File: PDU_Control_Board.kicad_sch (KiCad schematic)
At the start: 267 parts

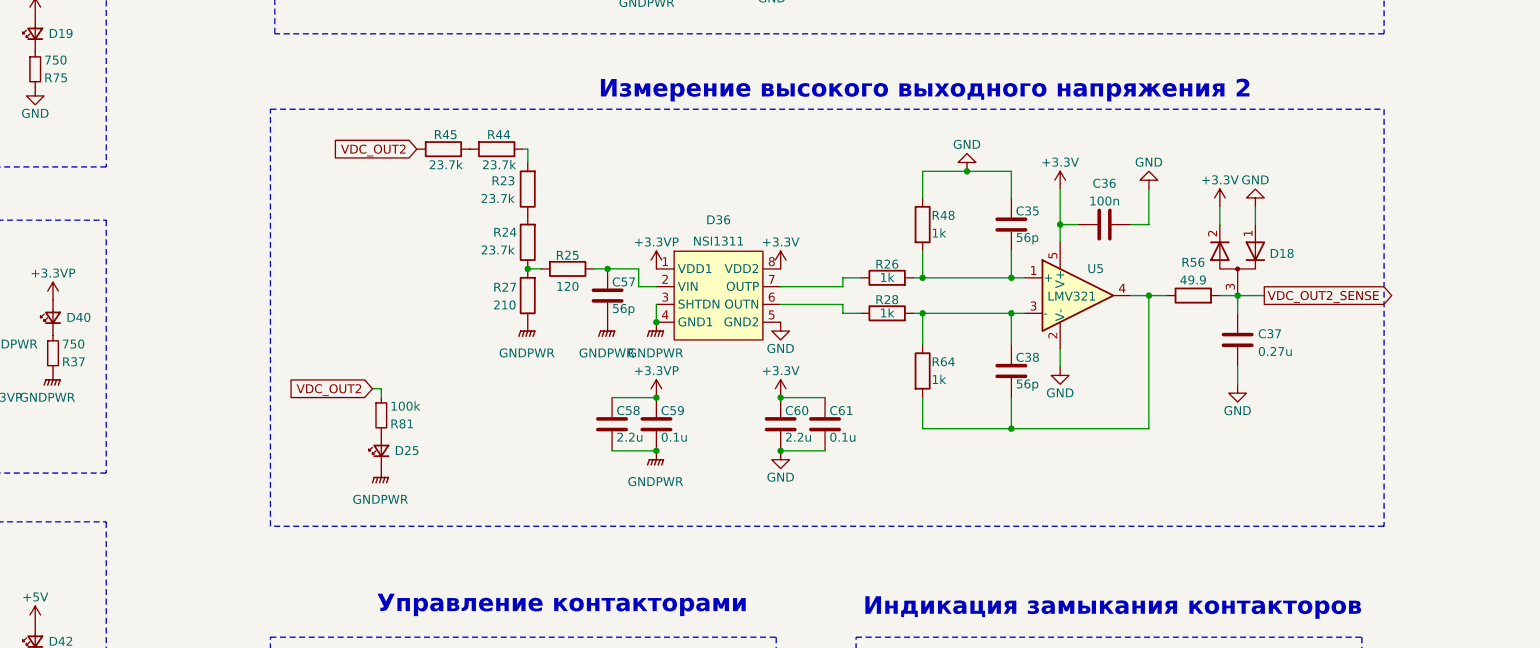
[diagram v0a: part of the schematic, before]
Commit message: VER1.1: добавил резистор смещение в измерение шины DC
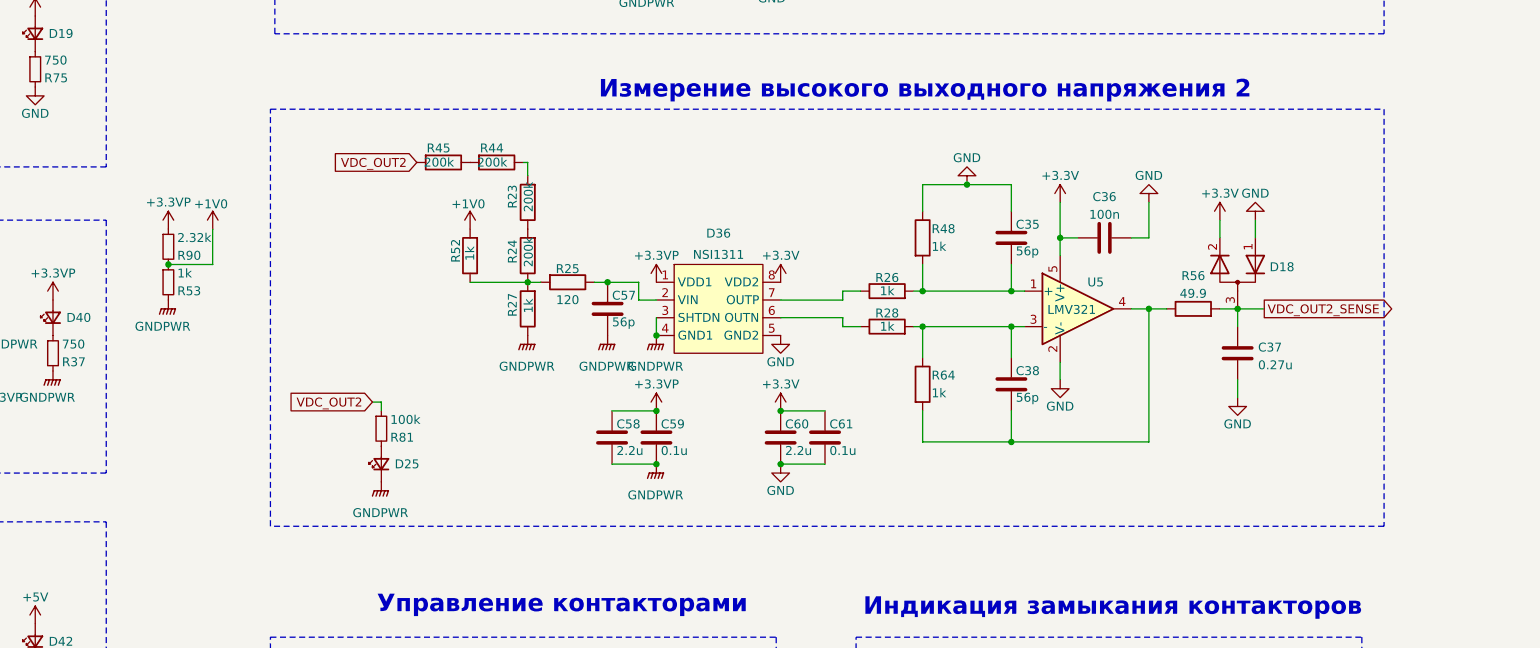
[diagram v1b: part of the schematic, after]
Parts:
- added R52: 1k, Resistor_SMD:R_1206_3216Metric, symbol Device:R
- added R53: 1k, Resistor_SMD:R_0805_2012Metric_Pad1.20x1.40mm_HandSolder, symbol Device:R_Small
- added R90: 2.32k, Resistor_SMD:R_0805_2012Metric_Pad1.20x1.40mm_HandSolder, symbol Device:R_Small
- R23, R24, R44, R45: value 23.7k -> 200k
- R27: value 210 -> 1k
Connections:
- net +3.3VP: now also R90.1
- net GNDPWR: now also R53.2
- net at R24.1, R25.2, R27.2: now also R52.1
- new net +1V0: R52.2, R53.1, R90.2
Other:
- moved on the sheet: C35, C36, C37, C38, C57, C58, C59, C60, C61, D18, D25, D36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

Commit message: VER1.2: добавил защиту по высокому
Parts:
- removed C77: 4.7u, Capacitor_SMD:C_1206_3216Metric_Pad1.33x1.80mm_HandSolder, symbol Device:C_Small
- removed C78, C79, C83: 10u, Capacitor_SMD:C_1206_3216Metric_Pad1.33x1.80mm_HandSolder, symbol Device:C_Small
- removed C80: 100n, Capacitor_SMD:C_0805_2012Metric_Pad1.18x1.45mm_HandSolder, symbol Device:C_Small
- removed C81, C82: 5.6n, Capacitor_SMD:C_0805_2012Metric_Pad1.18x1.45mm_HandSolder, symbol Device:C_Small
- removed D25, D26, D27: ~, LED_SMD:LED_0805_2012Metric, symbol Device:LED_Small
- removed D45: ~, MORNSUN:B_S-2WR3, symbol MORNSUN:A_S-2WR3
- removed D46: ~, Package_TO_SOT_SMD:SOT-23-5_HandSoldering, symbol Gate_Driver_my:RS8801HXF5
- removed D47, D48: D_Schottky_Small, symbol Device:D_Schottky_Small
- removed D49, D50: ~, Package_TO_SOT_THT:TO-220-2_Vertical, symbol Device:D_Schottky
- removed L2: 6.8u, symbol Device:L_Small
- removed L3: 560u, symbol Device:L
- removed Q12: ~, Package_TO_SOT_THT:TO-247-3_Vertical, symbol Transistor_FET:BSP129
- removed R55: 200, Resistor_SMD:R_0805_2012Metric_Pad1.20x1.40mm_HandSolder, symbol Device:R_Small
- removed R57: 13.3k, Resistor_SMD:R_0805_2012Metric_Pad1.20x1.40mm_HandSolder, symbol Device:R_Small
- removed R58: 200k, Resistor_SMD:R_0805_2012Metric_Pad1.20x1.40mm_HandSolder, symbol Device:R_Small
- removed R59: 2.37k, Resistor_SMD:R_0805_2012Metric_Pad1.20x1.40mm_HandSolder, symbol Device:R_Small
- removed R60, R63: 10k, Resistor_SMD:R_0805_2012Metric_Pad1.20x1.40mm_HandSolder, symbol Device:R_Small
- removed R61: 0.1, Resistor_SMD:R_2512_6332Metric_Pad1.40x3.35mm_HandSolder, symbol Device:R_Small
- removed R62: 0, Resistor_SMD:R_1206_3216Metric_Pad1.30x1.75mm_HandSolder, symbol Device:R_Small
- removed R81, R82, R83: 100k, Resistor_SMD:R_1206_3216Metric_Pad1.30x1.75mm_HandSolder, symbol Device:R_Small
- removed U7: ~, Package_TO_SOT_SMD:SOT-23-5_HandSoldering, symbol Comparator:LMV7219M5
- removed U8: ~, Package_TO_SOT_SMD:SOT-223-3_TabPin2, symbol Regulator_Linear:LD1117S33TR_SOT223
- added J15: ~, Connector_My:Mini-Fit_01x02_Vertical, symbol Connector_Generic:Conn_01x02
- added R55, R57: 1.6k, Resistor_SMD:R_1206_3216Metric, symbol Device:R
- C76: value 4.7u -> 100n; footprint Capacitor_SMD:C_1206_3216Metric_Pad1.33x1.80mm_HandSolder -> Capacitor_SMD:C_0805_2012Metric_Pad1.18x1.45mm_HandSolder
- R10, R11, R12, R13, R4, R5, R76, R77, R78, R79, R80: value 5.1k -> 8.2k
- R15, R16, R46, R49, R50, R51, R88, R89: value 23.7k -> 200k
- R18, R87: value 210 -> 1.6k
- R27, R52: value 1k -> 1.6k
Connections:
- net VDC_IN is gone; now on net VDC: J20.1 (Pin_1)
- net +1V0: now also C76.2, R55.2, R57.2
- net GND: no longer C76.2
- net GNDPWR: now also C76.1, J15.1 (Pin_1), J15.2 (Pin_2); no longer J20.2 (Pin_2), J21.2 (Pin_2), J22.2 (Pin_2)
- net VDC: now also J20.2 (Pin_2)
- net VDC_OUT1: now also J21.2 (Pin_2)
- net VDC_OUT2: now also J22.2 (Pin_2)
- net at R16.1, R17.2, R18.2: now also R55.1
- net at R86.2, R87.2, R88.1: now also R57.1
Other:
- note added: "Питание 1В"
- note removed: "Предзаряд электронный"
- moved on the sheet: C22, C23, C29, C30, C31, C32, C34, C47, C48, C49, C50, C51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

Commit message: VER1.2: отправил в резонит
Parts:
- D44: value BZT52C10 -> ~; Description P/N (none) -> Zener_Diode; Product Name (none) -> BZT52C10
- Q11: Product Name (none) -> 20N06
- R15, R16, R23, R24, R44, R45, R46, R49, R50, R51, R88, R89: value 200k -> 2M
- R18, R27, R52, R55, R57, R87: value 1.6k -> 16k
- R53: value 1k -> 100
- R90: value 2.32k -> 232
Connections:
- net Discete_8 is gone; now on net Discete_4: J14.8 (Pin_8), U2.46 (PE15)
- net Discete_1: now also J14.2 (Pin_2), U2.43 (PE12); no longer J14.1 (Pin_1), U2.39 (PE8)
- net Discete_2: now also J14.4 (Pin_4), U2.44 (PE13); no longer J14.2 (Pin_2), U2.40 (PE9)
- net Discete_3: now also J14.6 (Pin_6), U2.45 (PE14); no longer J14.3 (Pin_3), U2.41 (PE10)
- net Discete_4: no longer J14.4 (Pin_4), U2.42 (PE11)
- net GND: now also J14.1 (Pin_1), J14.3 (Pin_3), J14.5 (Pin_5), J14.7 (Pin_7)
- removed net Discete_5: J14.5 (Pin_5), U2.43 (PE12)
- removed net Discete_6: J14.6 (Pin_6), U2.44 (PE13)
- removed net Discete_7: J14.7 (Pin_7), U2.45 (PE14)
- no-connect marks 53 -> 57

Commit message: VER1.2: добавил КД на диск
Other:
- note added: "1. Перечень элементов см. НВЦТ.0001.0400.200 ПЭ3_v1.2"
- note added: "НВЦТ.0001.0400.200"
- note added: "ООО "Электротранспортные"
- note added: "Разъемы и механические отверстия"
- note added: "Схема электрическая принципиальная"
- note added: "технологии""
- title: (none) -> Плата управления
- moved on the sheet: C1, C10, C11, C12, C13, C14, C15, C16, C17, C18, C19, C2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

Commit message: VER1.2: исправил доки
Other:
- note added: "1. Перечень элементов см. НВЦТ.0001.0400.200 ПЭ3_v1."
- note added: "НВЦТ.0001.0400.200_v1"
- note removed: "1. Перечень элементов см. НВЦТ.0001.0400.200 ПЭ3_v1.2"
- note removed: "НВЦТ.0001.0400.200"
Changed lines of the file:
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@@
 	(title_block
 		(title "Плата управления")
-		(comment 1 "НВЦТ.0001.0400.200 Э3_v1.2")
+		(comment 1 "НВЦТ.0001.0400.200 Э3_v1 Э3")
 		(comment 2 "Филатов А.С,")
 		(comment 3 "Сизякин.А.В.")
@@
 		)
 	)
-	(text "НВЦТ.0001.0400.200"
+	(text "НВЦТ.0001.0400.200_v1"
 		(exclude_from_sim no)
 		(at 16.764 333.502 90)
@@
 		)
 	)
-	(text "1. Перечень элементов см. НВЦТ.0001.0400.200 ПЭ3_v1.2"
+	(text "1. Перечень элементов см. НВЦТ.0001.0400.200 ПЭ3_v1."
 		(exclude_from_sim no)
 		(at 697.738 508.254 0)

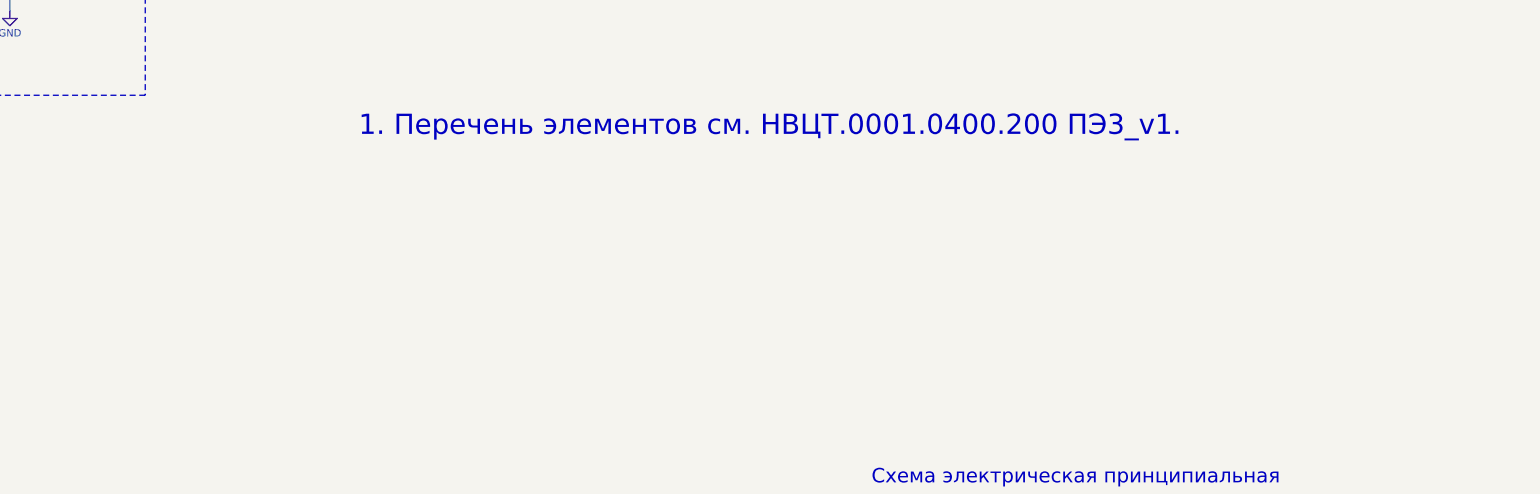
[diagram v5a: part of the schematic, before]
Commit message: VER1.2: исправил ошибки в доках
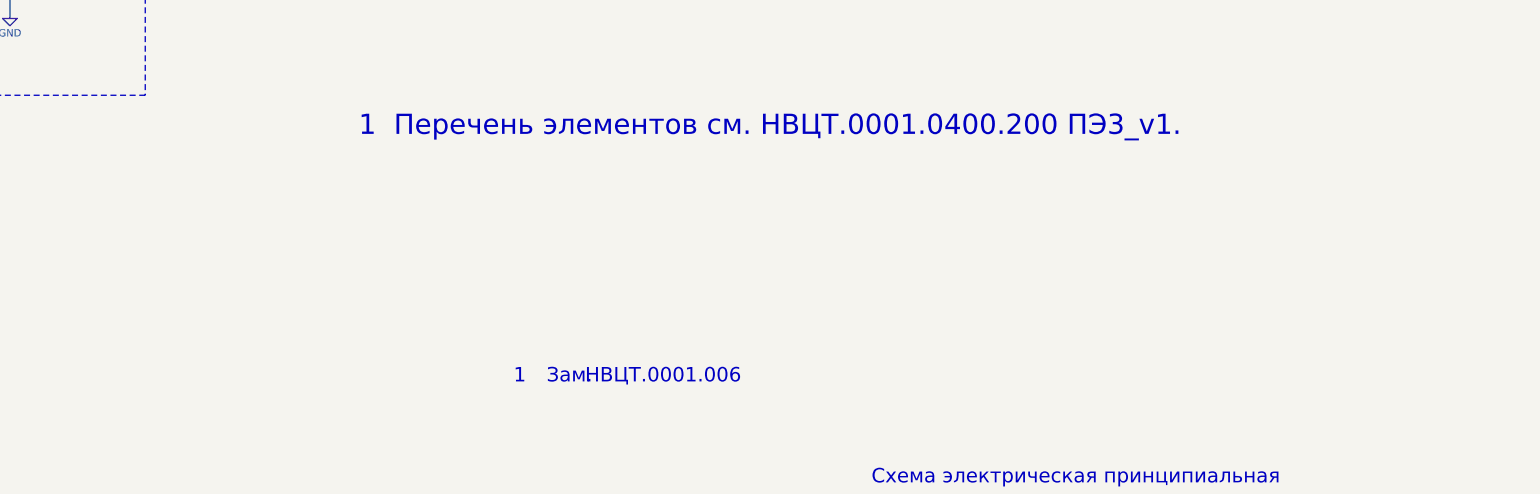
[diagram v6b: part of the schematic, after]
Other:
- note added: "1"
- note added: "1 Перечень элементов см. НВЦТ.0001.0400.200 ПЭ3_v1."
- note added: "Зам."
- note added: "НВЦТ.0001.006"
- note removed: "1. Перечень элементов см. НВЦТ.0001.0400.200 ПЭ3_v1."
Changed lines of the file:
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@@
 	(title_block
 		(title "Плата управления")
-		(comment 1 "НВЦТ.0001.0400.200 Э3_v1 Э3")
+		(comment 1 "НВЦТ.0001.0400.200_v1 Э3")
 		(comment 2 "Филатов А.С,")
 		(comment 3 "Сизякин.А.В.")
@@
 		)
 	)
+	(text "1"
+		(exclude_from_sim no)
+		(at 654.304 551.688 0)
+		(effects
+			(font
+				(size 2.5 2.5)
+			)
+		)
+	)
 	(text "Питание МК"
 		(exclude_from_sim no)
@@
 		)
 	)
+	(text "НВЦТ.0001.006\n"
+		(exclude_from_sim no)
+		(at 679.196 551.688 0)
+		(effects
+			(font
+				(size 2.5 2.5)
+			)
+		)
+	)
 	(text "Измерение высокого входного напряжения "
 		(exclude_from_sim no)
@@
 		)
 	)
-	(text "1. Перечень элементов см. НВЦТ.0001.0400.200 ПЭ3_v1."
+	(text "1  Перечень элементов см. НВЦТ.0001.0400.200 ПЭ3_v1."
 		(exclude_from_sim no)
 		(at 697.738 508.254 0)
@@
 			)
 		)
+	)
+	(text "Зам."
+		(exclude_from_sim no)
+		(at 662.94 551.688 0)
+		(effects
+			(font
+				(size 2.5 2.5)
+			)
+		)
